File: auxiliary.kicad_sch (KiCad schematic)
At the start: 15 parts, among them J7 Conn_01x05, Y1 32.768KHZ, Y2 X322525MOB4SI-25MHz

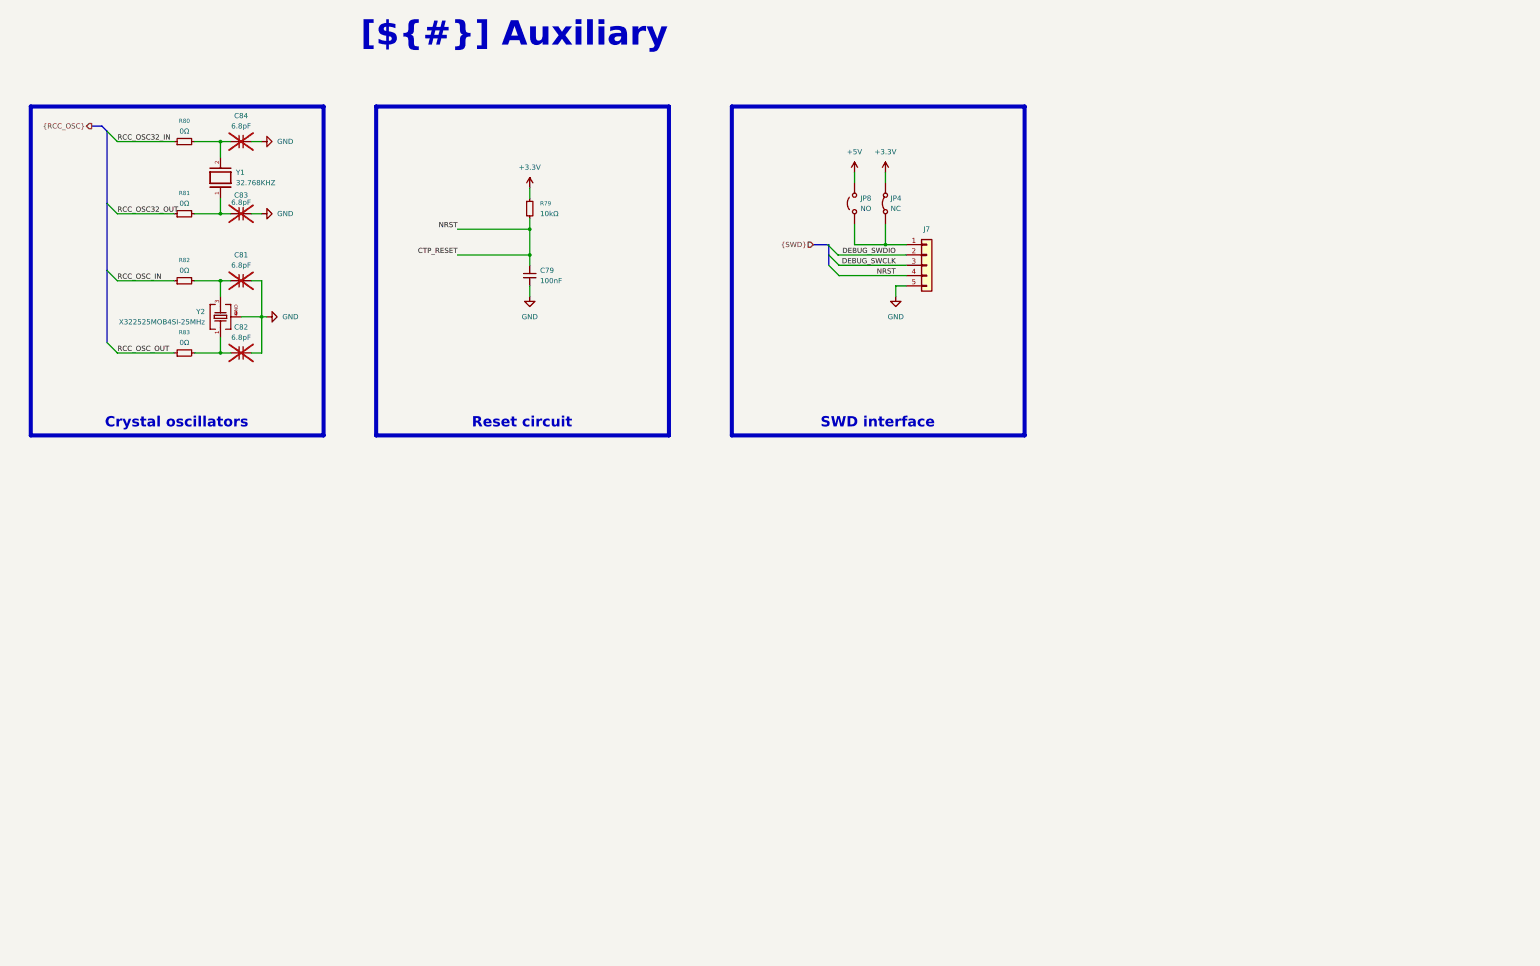
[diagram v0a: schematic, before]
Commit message: added gpio expander, uc pinout, unused gpio connector, i2c pullup, delete unused files
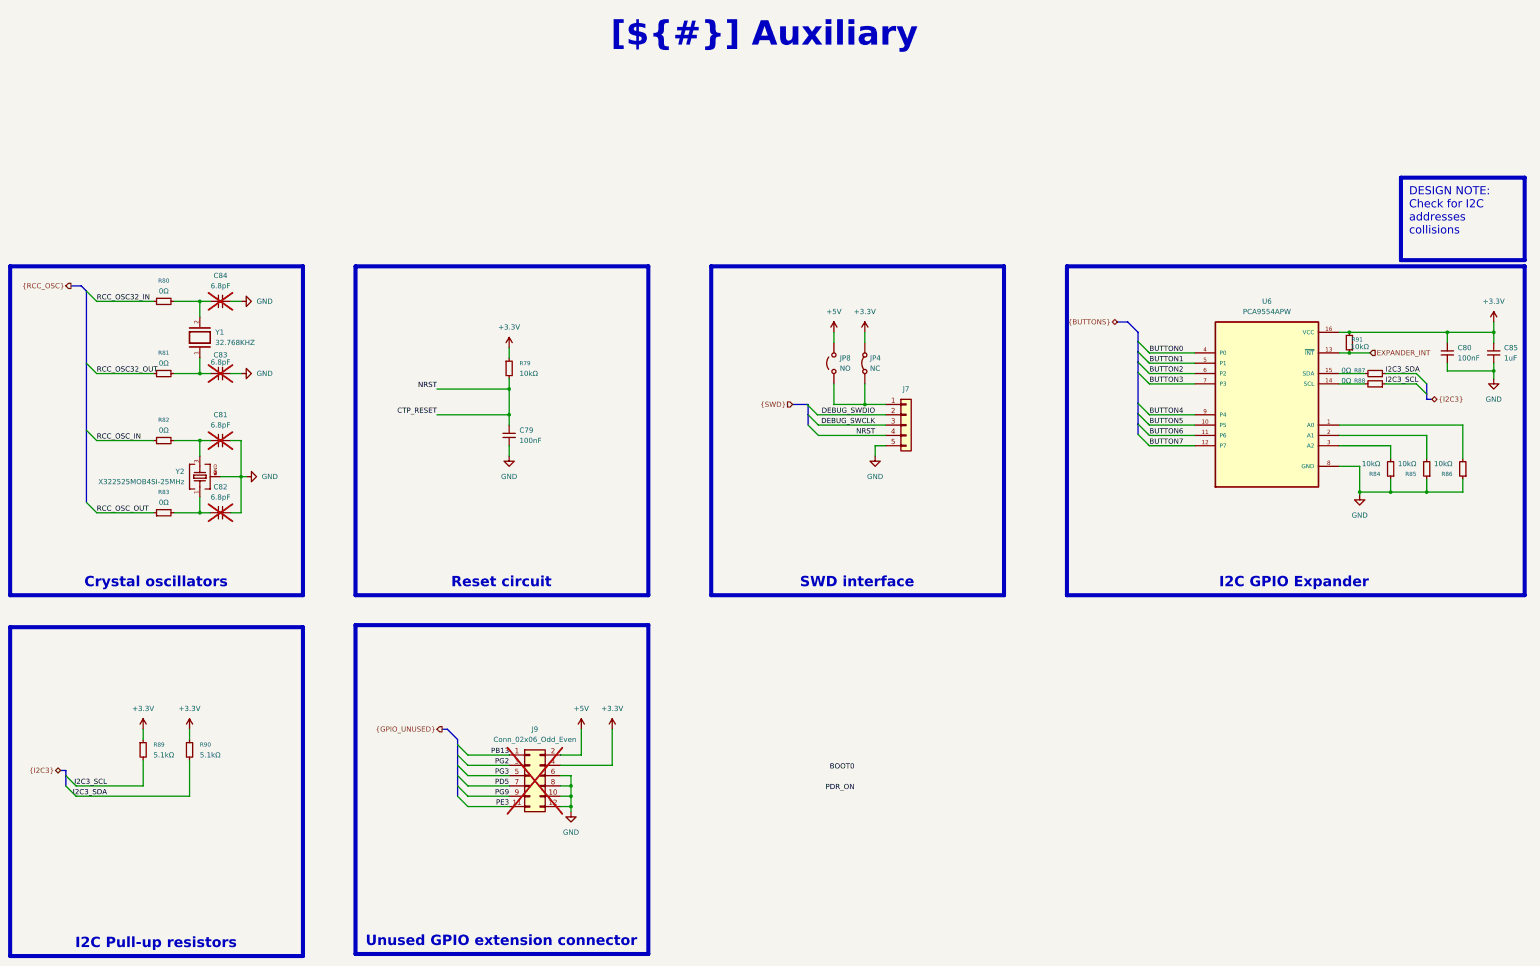
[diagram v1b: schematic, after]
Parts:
- added C80: 100nF, 0_capacitors:C_0402_1005Metric, symbol 0_capacitors:CL05B104KO5NNNC
- added C85: 1uF, 0_capacitors:C_0603_1608Metric, symbol 0_capacitors:CL10A105KB8NNNC
- added J9: Conn_02x06_Odd_Even, symbol Connector_Generic:Conn_02x06_Odd_Even
- added R84, R85, R86, R91: 10kΩ, 0_resistors:R_0402_1005Metric, symbol 0_resistors:0402WGF1002TCE
- added R87, R88: 0Ω, 0_resistors:R_0402_1005Metric, symbol 0_resistors:0402WGF0000TCE
- added R89, R90: 5.1kΩ, 0_resistors:R_0402_1005Metric, symbol 0_resistors:0402WGF5101TCE
- added U6: PCA9554APW, 0_integrated_circuits:SOP65P640X120-16N, symbol 0_integrated_circuits:PCA9554APW
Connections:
- net +3.3V: now also C80.1, C85.1, J9.4 (Pin_4), R89.1, R90.1, R91.2, U6.16 (VCC)
- net +5V: now also J9.2 (Pin_2)
- net GND: now also C80.2, C85.2, J9.10 (Pin_10), J9.12 (Pin_12), J9.6 (Pin_6), J9.8 (Pin_8), R84.1, R85.1, R86.1, U6.8 (GND)
- new net: R88.2, U6.14 (SCL)
- new net: R86.2, U6.1 (A0)
- new net: R87.2, U6.15 (SDA)
- new net: R85.2, U6.2 (A1)
- new net: R84.2, U6.3 (A2)
- new net BUTTON0: U6.4 (P0)
- new net BUTTON1: U6.5 (P1)
- new net BUTTON2: U6.6 (P2)
- new net BUTTON3: U6.7 (P3)
- new net BUTTON4: U6.9 (P4)
- new net BUTTON5: U6.10 (P5)
- new net BUTTON6: U6.11 (P6)
- new net BUTTON7: U6.12 (P7)
- new net EXPANDER_INT: R91.1, U6.13 (~{INT})
- new net I2C3_SCL: R88.1, R89.2
- new net I2C3_SDA: R87.1, R90.2
- new net PB13: J9.1 (Pin_1)
- new net PD5: J9.7 (Pin_7)
- new net PE3: J9.11 (Pin_11)
- new net PG2: J9.3 (Pin_3)
- new net PG3: J9.5 (Pin_5)
- new net PG9: J9.9 (Pin_9)
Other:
- moved on the sheet: C79, C81, C82, C83, C84, J7, JP4, JP8, R79, R80, R81, R82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

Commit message: added 2pin 2.54 male header and connect boot0, pdr_on signals
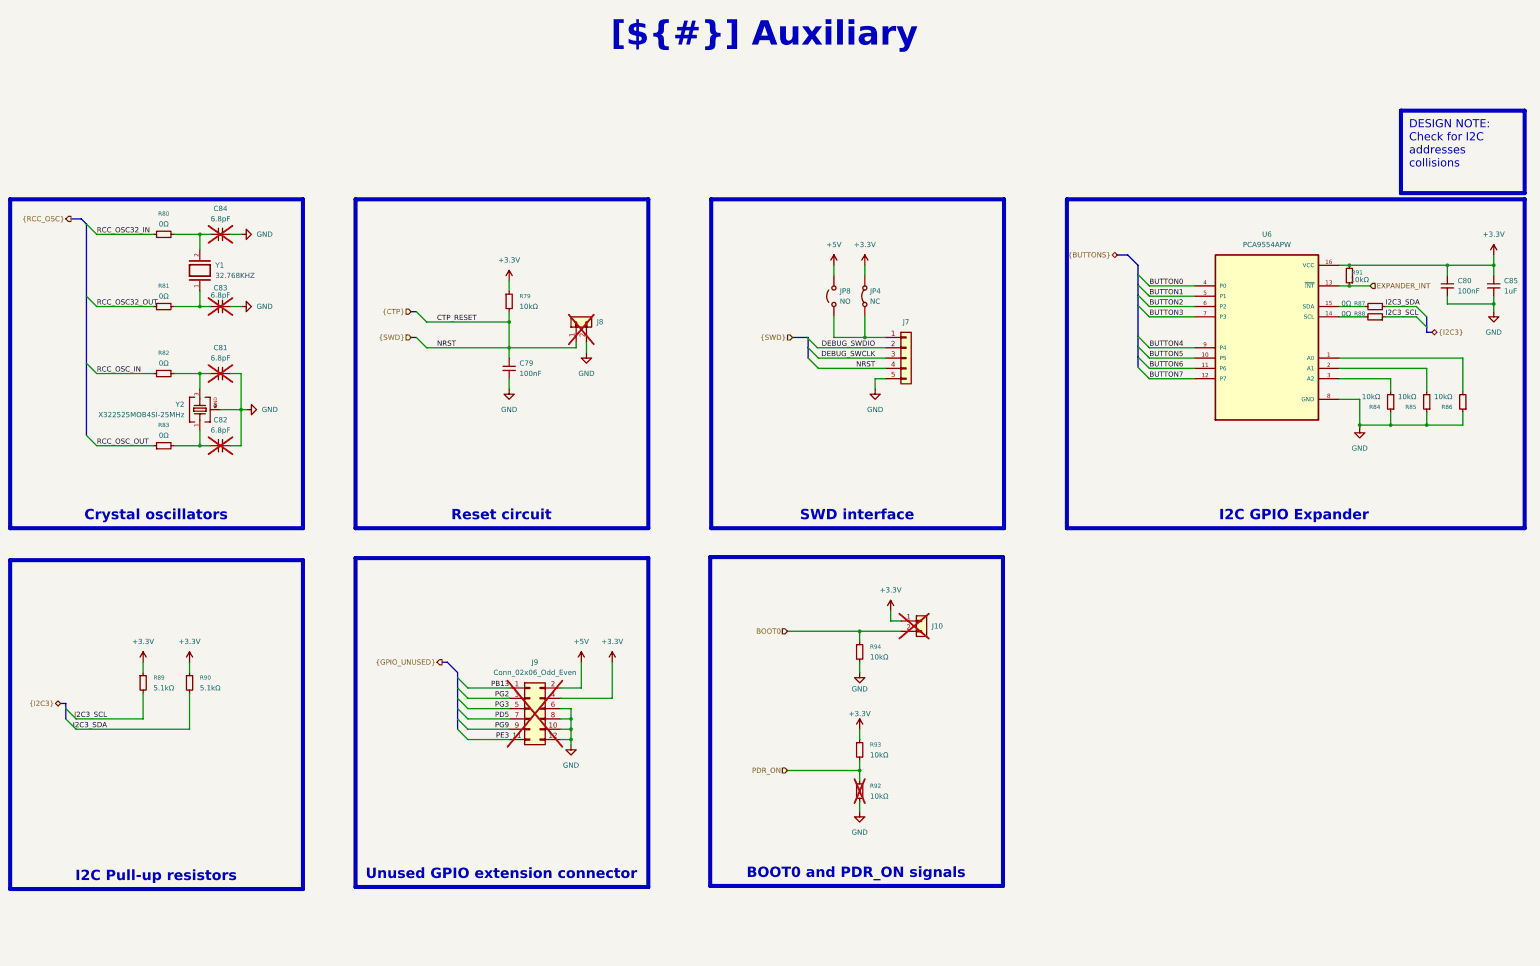
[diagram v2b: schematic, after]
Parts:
- added J10, J8: ~, Connector_PinHeader_2.54mm:PinHeader_1x02_P2.54mm_Vertical, symbol 0_connectors:2.54mm 2pin male header
- added R92, R93, R94: 10kΩ, 0_resistors:R_0402_1005Metric, symbol 0_resistors:0402WGF1002TCE
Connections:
- net +3.3V: now also J10.1 (Pin_1), R93.1
- net BOOT0: now also J10.2 (Pin_2), R94.1
- net CTP_RESET: now also J8.1 (Pin_1)
- net GND: now also J8.2 (Pin_2), R92.2, R94.2
- net PDR_ON: now also R92.1, R93.2
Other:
- moved on the sheet: C79, C80, C81, C82, C83, C84, C85, J7, J9, JP4, JP8, R79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

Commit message: update project structure and import to pcb
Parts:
- J9: footprint (none) -> Connector_PinSocket_2.54mm:PinSocket_2x06_P2.54mm_Vertical
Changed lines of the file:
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@@
 			)
 		)
-		(property "Footprint" ""
+		(property "Footprint" "Connector_PinSocket_2.54mm:PinSocket_2x06_P2.54mm_Vertical"
 			(at 152.4 185.42 0)
 			(effects
@@
 			(at 152.4 185.42 0)
 			(effects
+				(font
+					(size 1.27 1.27)
+				)
+				(hide yes)
+			)
+		)
+		(property "Supplier 1" ""
+			(at 152.4 185.42 0)
+			(effects
+				(font
+					(size 1.27 1.27)
+				)
+				(hide yes)
+			)
+		)
+		(property "Supplier Part Number 1" ""
+			(at 152.4 185.42 0)
+			(effects

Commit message: change 32.768kHz footrpint
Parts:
- Y1: footprint 0_oscillators:X322525MOB4SI 25MHz -> 0_oscillators:Q13FC13500004-32.768KHZ-4-T
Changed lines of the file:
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@@
 			)
 		)
-		(property "Footprint" "0_oscillators:X322525MOB4SI 25MHz"
+		(property "Footprint" "0_oscillators:Q13FC13500004-32.768KHZ-4-T"
 			(at 71.12 77.47 0)
 			(effects

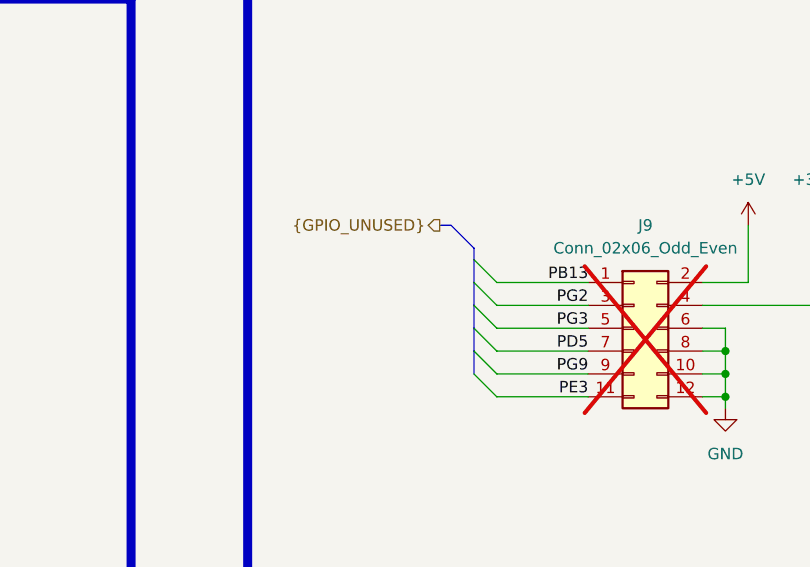
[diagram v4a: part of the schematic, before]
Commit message: duzo zmian, layout przetwornic i zasilania, wstepny routing sd card impedance control, usb differential impedance control
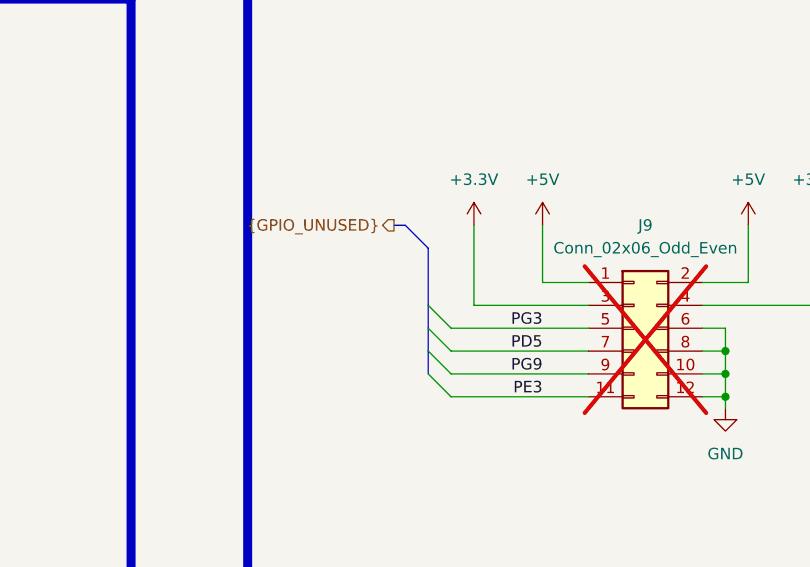
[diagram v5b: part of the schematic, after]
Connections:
- net PB13 is gone; now on net +5V: J9.1 (Pin_1)
- net PG2 is gone; now on net +3.3V: J9.3 (Pin_3)
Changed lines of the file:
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@@
 	)
 	(bus_entry
-		(at 134.62 177.8)
-		(size 2.54 2.54)
-		(stroke
-			(width 0)
-			(type default)
-		)
-	)
-	(bus_entry
 		(at 302.26 93.726)
 		(size 2.54 2.54)
@@
 	)
 	(bus_entry
-		(at 134.62 182.88)
+		(at 129.54 182.88)
 		(size 2.54 2.54)
 		(stroke
@@
 	)
 	(bus_entry
-		(at 134.62 190.5)
+		(at 129.54 190.5)
 		(size 2.54 2.54)
 		(stroke
@@
 	)
 	(bus_entry
-		(at 134.62 180.34)
-		(size 2.54 2.54)
-		(stroke
-			(width 0)
-			(type default)
-		)
-	)
-	(bus_entry
 		(at 302.26 96.266)
 		(size 2.54 2.54)
@@
 	)
 	(bus_entry
-		(at 134.62 187.96)
+		(at 129.54 187.96)
 		(size 2.54 2.54)
 		(stroke
@@
 	)
 	(bus_entry
-		(at 134.62 185.42)
+		(at 129.54 185.42)
 		(size 2.54 2.54)
 		(stroke
@@
 	(wire
 		(pts
-			(xy 137.16 182.88) (xy 147.32 182.88)
-		)
-		(stroke
-			(width 0)
-			(type default)
-		)
-	)
-	(wire
-		(pts
 			(xy 71.12 68.58) (xy 71.12 72.39)
 		)
@@
 		)
 	)
-	(bus
-		(pts
-			(xy 134.62 180.34) (xy 134.62 182.88)
-		)
-		(stroke
-			(width 0)
-			(type default)
-		)
-	)
 	(wire
 		(pts
@@
 	(bus
 		(pts
-			(xy 134.62 185.42) (xy 134.62 187.96)
+			(xy 129.54 185.42) (xy 129.54 187.96)
 		)
 		(stroke
@@
 	(wire
 		(pts
-			(xy 137.16 190.5) (xy 147.32 190.5)
+			(xy 132.08 190.5) (xy 147.32 190.5)
 		)
 		(stroke
@@
 	(bus
 		(pts
-			(xy 130.81 173.99) (xy 132.08 173.99)
+			(xy 125.73 173.99) (xy 127 173.99)
 		)
 		(stroke
@@
 	(wire
 		(pts
-			(xy 137.16 193.04) (xy 147.32 193.04)
+			(xy 132.08 193.04) (xy 147.32 193.04)
 		)
 		(stroke
@@
 		)
 	)
+	(wire
+		(pts
+			(xy 142.24 173.99) (xy 142.24 180.34)
+		)
+		(stroke
+			(width 0)
+			(type default)
+		)
+	)
+	(wire
+		(pts
+			(xy 147.32 180.34) (xy 142.24 180.34)
+		)
+		(stroke
+			(width 0)
+			(type default)
+		)
+	)
 	(bus
 		(pts
@@
 		)
 	)
-	(bus
-		(pts
-			(xy 134.62 176.53) (xy 134.62 177.8)
-		)
-		(stroke
-			(width 0)
-			(type default)
-		)
-	)
 	(wire
 		(pts
@@
 	(wire
 		(pts
-			(xy 137.16 187.96) (xy 147.32 187.96)
+			(xy 132.08 187.96) (xy 147.32 187.96)
 		)
 		(stroke
@@
 	(bus
 		(pts
-			(xy 134.62 177.8) (xy 134.62 180.34)
+			(xy 129.54 176.53) (xy 129.54 182.88)
 		)
 		(stroke
@@
 	(bus
 		(pts
-			(xy 132.08 173.99) (xy 134.62 176.53)
+			(xy 127 173.99) (xy 129.54 176.53)
 		)
 		(stroke
@@
 	(wire
 		(pts
-			(xy 137.16 185.42) (xy 147.32 185.42)
+			(xy 132.08 185.42) (xy 147.32 185.42)
 		)
 		(stroke
@@
 	(bus
 		(pts
-			(xy 134.62 187.96) (xy 134.62 190.5)
+			(xy 129.54 187.96) (xy 129.54 190.5)
 		)
 		(stroke
@@
 		)
 	)
+	(wire
+		(pts
+			(xy 134.62 173.99) (xy 134.62 182.88)
+		)
+		(stroke
+			(width 0)
+			(type default)
+		)
+	)
 	(bus
 		(pts
@@
 	(wire
 		(pts
-			(xy 137.16 180.34) (xy 147.32 180.34)
+			(xy 147.32 182.88) (xy 134.62 182.88)
 		)
 		(stroke
@@
 	(bus
 		(pts
-			(xy 134.62 182.88) (xy 134.62 185.42)
+			(xy 129.54 182.88) (xy 129.54 185.42)
 		)
 		(stroke
@@
 		)
 	)
-	(label "PG2"
-		(at 147.32 182.88 180)
-		(effects
-			(font
-				(size 1.27 1.27)
-			)
-			(justify right bottom)
-		)
-	)
 	(label "BUTTON0"
 		(at 305.054 81.28 0)
@@
 	)
 	(label "PD5"
-		(at 147.32 187.96 180)
+		(at 142.24 187.96 180)
 		(effects
 			(font
@@
 		)
 	)
-	(label "PB13"
-		(at 147.32 180.34 180)
-		(effects
-			(font
-				(size 1.27 1.27)
-			)
-			(justify right bottom)
-		)
-	)
 	(label "CTP_RESET"
 		(at 129.54 90.17 0)
@@
 	)
 	(label "PG9"
-		(at 147.32 190.5 180)
+		(at 142.24 190.5 180)
 		(effects
 			(font
@@
 	)
 	(label "PE3"
-		(at 147.32 193.04 180)
+		(at 142.24 193.04 180)
 		(effects
 			(font
@@
 	)
 	(label "PG3"
-		(at 147.32 185.42 180)
+		(at 142.24 185.42 180)
 		(effects
 			(font
@@
 	(hierarchical_label "{GPIO_UNUSED}"
 		(shape output)
-		(at 130.81 173.99 180)
+		(at 125.73 173.99 180)
 		(effects
 			(font
@@
 	)
 	(symbol
+		(lib_id "power:+3.3V")
+		(at 134.62 173.99 0)
+		(mirror y)
+		(unit 1)
+		(exclude_from_sim no)
+		(in_bom yes)
+		(on_board yes)
+		(dnp no)
+		(fields_autoplaced yes)
+		(property "Reference" "#PWR0174"
+			(at 134.62 177.8 0)
+			(effects
+				(font
+					(size 1.27 1.27)
+				)
+				(hide yes)
+			)
+		)
+		(property "Value" "+3.3V"
+			(at 134.62 168.91 0)
+			(effects
+				(font
+					(size 1.27 1.27)
+				)
+			)
+		)
+		(property "Footprint" ""
+			(at 134.62 173.99 0)
+			(effects
+				(font
+					(size 1.27 1.27)
+				)
+				(hide yes)
+			)
+		)
+		(property "Datasheet" ""
+			(at 134.62 173.99 0)
+			(effects
+				(font
+					(size 1.27 1.27)
+				)
+				(hide yes)
+			)
+		)
+		(property "Description" "Power symbol creates a global label with name \"+3.3V\""
+			(at 134.62 173.99 0)
+			(effects
+				(font
+					(size 1.27 1.27)
+				)
+				(hide yes)
+			)
+		)
+		(pin "1"
+		)
+		(instances
+			(project "transmitter"
+				(path "/0650c7a8-acba-429c-9f8e-eec0baf0bc1c/fede4c36-00cc-4d3d-b71c-5243ba232202/2ce35fe4-ba06-41c1-96ff-d5b98e0c7ab9"
+					(reference "#PWR0174")
+					(unit 1)
+				)
+			)
+		)
+	)
+	(symbol
 		(lib_id "0_capacitors:CL10A105KB8NNNC")
 		(at 389.89 81.28 0)
@@
 					(unit 1)
 				)
+			)
+		)
+	)
+	(symbol
+		(lib_id "power:+5V")
+		(at 142.24 173.99 0)
+		(mirror y)
+		(unit 1)
+		(exclude_from_sim no)
+		(in_bom yes)
+		(on_board yes)
+		(dnp no)
+		(fields_autoplaced yes)
+		(property "Reference" "#PWR0173"
+			(at 142.24 177.8 0)
+			(effects
+				(font
+					(size 1.27 1.27)
+				)
+				(hide yes)
+			)
+		)
+		(property "Value" "+5V"
+			(at 142.24 168.91 0)
+			(effects
+				(font
+					(size 1.27 1.27)
+				)
+			)
+		)
+		(property "Footprint" ""
+			(at 142.24 173.99 0)
+			(effects
+				(font
+					(size 1.27 1.27)
+				)
+				(hide yes)
+			)
+		)
+		(property "Datasheet" ""
+			(at 142.24 173.99 0)
+			(effects
+				(font
+					(size 1.27 1.27)
+				)
+				(hide yes)
+			)
+		)
+		(property "Description" "Power symbol creates a global label with name \"+5V\""
+			(at 142.24 173.99 0)
+			(effects
+				(font
+					(size 1.27 1.27)
+				)
+				(hide yes)
+			)
+		)
+		(pin "1"
+		)
+		(instances
+			(project "transmitter"
+				(path "/0650c7a8-acba-429c-9f8e-eec0baf0bc1c/fede4c36-00cc-4d3d-b71c-5243ba232202/2ce35fe4-ba06-41c1-96ff-d5b98e0c7ab9"
+					(reference "#PWR0173")
+					(unit 1)
+				)

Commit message: lcd connector routing
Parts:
- J10: footprint Connector_PinHeader_2.54mm:PinHeader_1x02_P2.54mm_Vertical -> Connector_PinHeader_2.00mm:PinHeader_1x02_P2.00mm_Vertical
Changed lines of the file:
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@@
 			)
 		)
-		(property "Footprint" "Connector_PinHeader_2.54mm:PinHeader_1x02_P2.54mm_Vertical"
+		(property "Footprint" "Connector_PinHeader_2.00mm:PinHeader_1x02_P2.00mm_Vertical"
 			(at 248.92 163.83 0)
 			(effects

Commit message: qspi layout, length matching, sdcard lengthmatching, change some footprints, prototype production generation
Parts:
- J10: Supplier Part Number 1 C492401 -> C541856
- J8: footprint Connector_PinHeader_2.54mm:PinHeader_1x02_P2.54mm_Vertical -> Connector_PinHeader_2.00mm:PinHeader_1x02_P2.00mm_Vertical; Supplier Part Number 1 C492401 -> C541856
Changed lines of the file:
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@@
 			)
 		)
-		(property "Supplier Part Number 1" "C492401"
+		(property "Supplier Part Number 1" "C541856"
 			(at 248.92 163.83 0)
 			(effects
@@
 			)
 		)
-		(property "Footprint" "Connector_PinHeader_2.54mm:PinHeader_1x02_P2.54mm_Vertical"
+		(property "Footprint" "Connector_PinHeader_2.00mm:PinHeader_1x02_P2.00mm_Vertical"
 			(at 163.83 90.17 0)
 			(effects
@@
 			)
 		)
-		(property "Supplier Part Number 1" "C492401"
+		(property "Supplier Part Number 1" "C541856"
 			(at 163.83 90.17 0)
 			(effects
